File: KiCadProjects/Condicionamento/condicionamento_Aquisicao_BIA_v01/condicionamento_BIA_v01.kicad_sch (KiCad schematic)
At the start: 27 parts, among them J1 Vref, J2 tensoes, J3 sinais analogicos, J4 comunicacao / sinais digitais, J5 sinais_condicionados, J6 alimetacao_Master, J7 Eletrodos, U1 AD828AN, U2 BluePill_STM32F103C, U3 BluePill_STM32F103C

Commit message: Esquemático
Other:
- title: Condicionamento 2 canais duplicado -> Condicionamento 2 canais 
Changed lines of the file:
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@@
   (paper "A4")
   (title_block
-    (title "Condicionamento 2 canais duplicado")
+    (title "Condicionamento 2 canais ")
     (date "2023-07-17")
     (rev "v01")

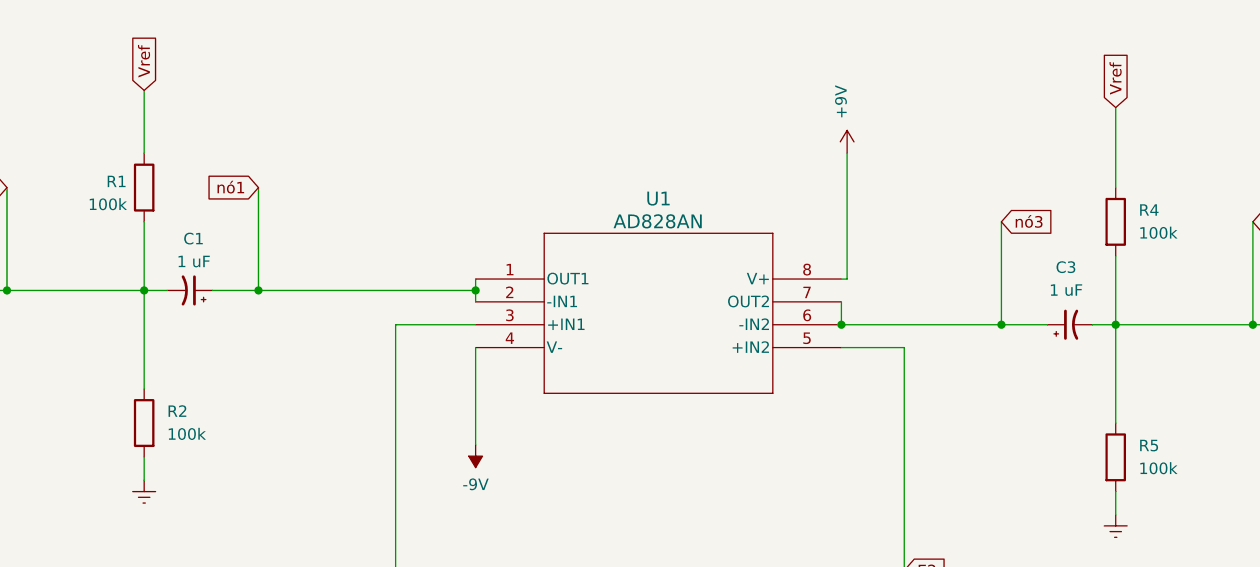
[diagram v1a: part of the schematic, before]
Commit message: correção polaridade capacitor condicionamento
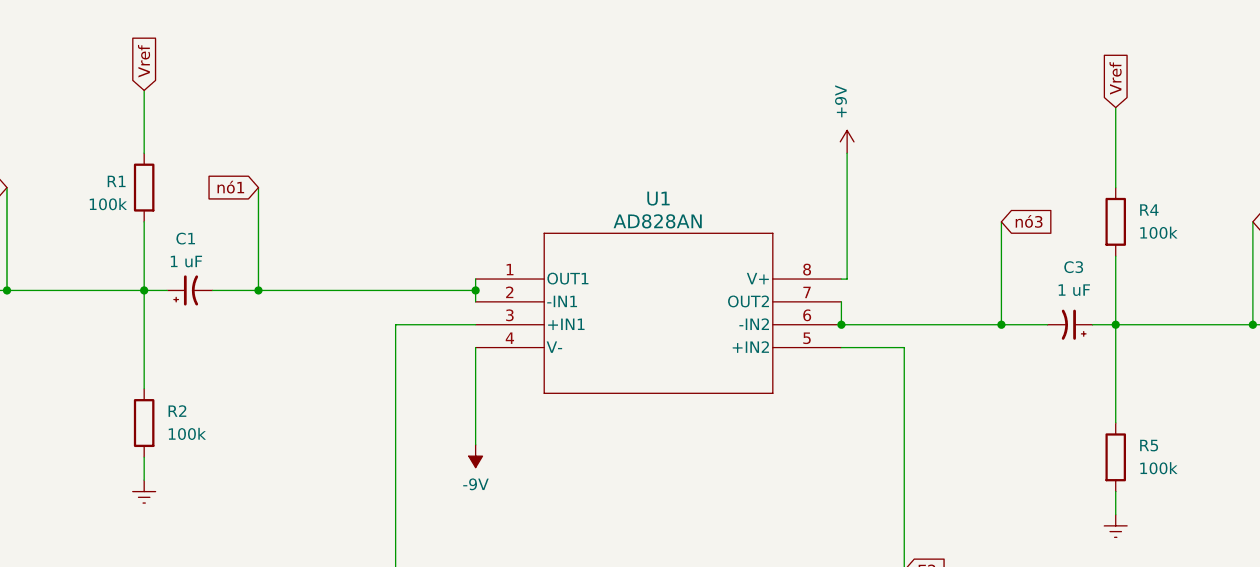
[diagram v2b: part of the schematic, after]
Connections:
- net nó1: now also C1.2; no longer C1.1
- net nó2: now also C1.1; no longer C1.2
- net nó3: now also C3.2; no longer C3.1
- net nó4: now also C3.1; no longer C3.2
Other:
- moved on the sheet: C1, C3
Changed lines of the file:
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@@
     )
   )
-  (symbol (lib_id "Device:C_Polarized_Small_US") (at 97.79 113.03 270) (mirror x) (unit 1)
-    (in_bom yes) (on_board yes) (dnp no) (fields_autoplaced)
-    (property "Reference" "C1" (at 98.2218 107.315 90)
-      (effects (font (size 1.27 1.27)))
-    )
-    (property "Value" "1 uF" (at 98.2218 109.855 90)
+  (symbol (lib_id "Device:C_Polarized_Small_US") (at 97.79 113.03 90) (unit 1)
+    (in_bom yes) (on_board yes) (dnp no)
+    (property "Reference" "C1" (at 97.3582 107.315 90)
+      (effects (font (size 1.27 1.27)))
+    )
+    (property "Value" "1 uF" (at 97.3582 109.855 90)
       (effects (font (size 1.27 1.27)))
     )
@@
     )
   )
-  (symbol (lib_id "Device:C_Polarized_Small_US") (at 195.58 116.84 90) (unit 1)
-    (in_bom yes) (on_board yes) (dnp no) (fields_autoplaced)
-    (property "Reference" "C3" (at 195.1482 110.49 90)
-      (effects (font (size 1.27 1.27)))
-    )
-    (property "Value" "1 uF" (at 195.1482 113.03 90)
-      (effects (font (size 1.27 1.27)))
-    )
+  (symbol (lib_id "Device:C_Polarized_Small_US") (at 195.58 116.84 270) (mirror x) (unit 1)
+    (in_bom yes) (on_board yes) (dnp no)
+    (property "Reference" "C3" (at 196.0118 110.49 90)
+      (effects (font (size 1.27 1.27)))
+    )
+    (property "Value" "1 uF" (at 196.0118 113.03 90)
+      (effects (font (size 1.27 1.27)))
+    )
